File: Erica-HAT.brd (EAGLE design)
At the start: 65 x 56 mm, 64 parts, among them IC1 MEGA8-AI, K1 PIN20X2, Q1 12M, Q2 2.5A/30V, U1 EEPROM24, U2 TMP102, U3 AD5241BRZ1M, U4 MMDT2907A-7-F, U5 +12v

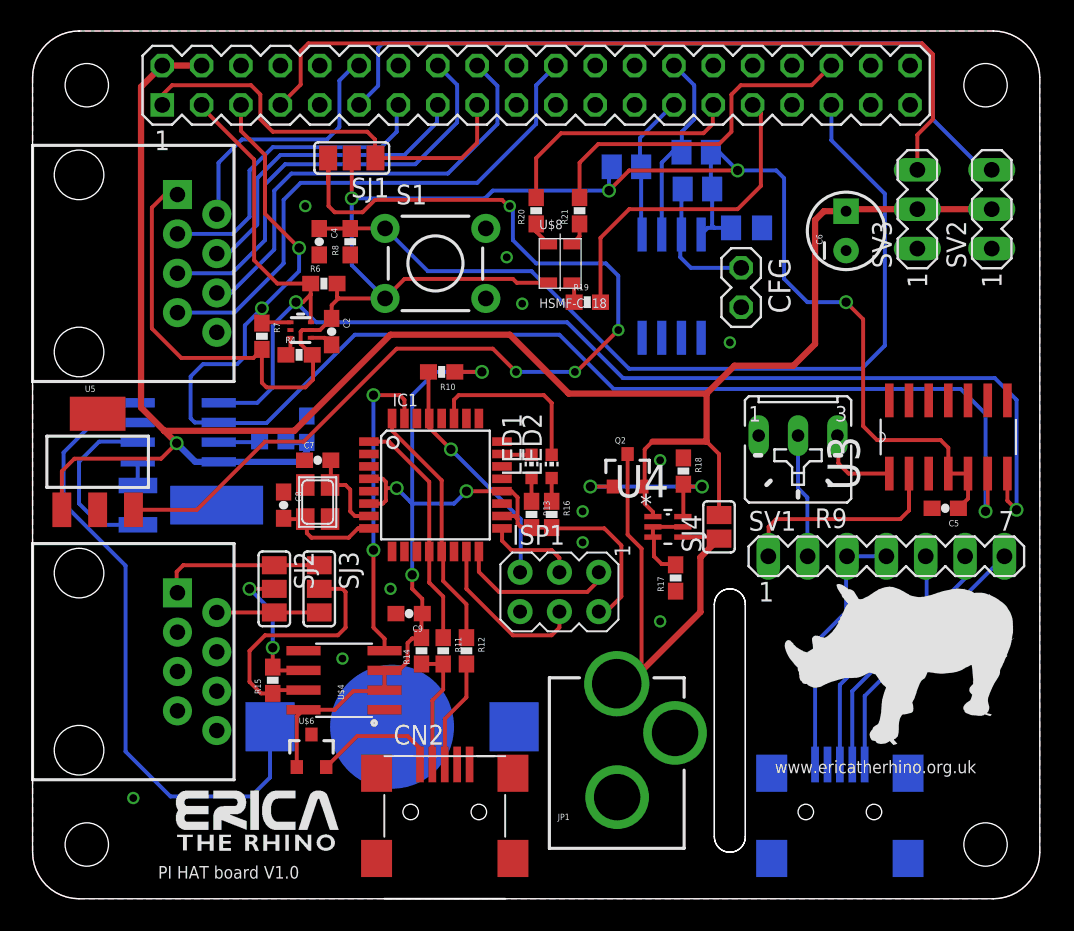
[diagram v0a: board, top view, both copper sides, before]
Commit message: Fixed remaining air wires. Added additional stitching. DRC clean.
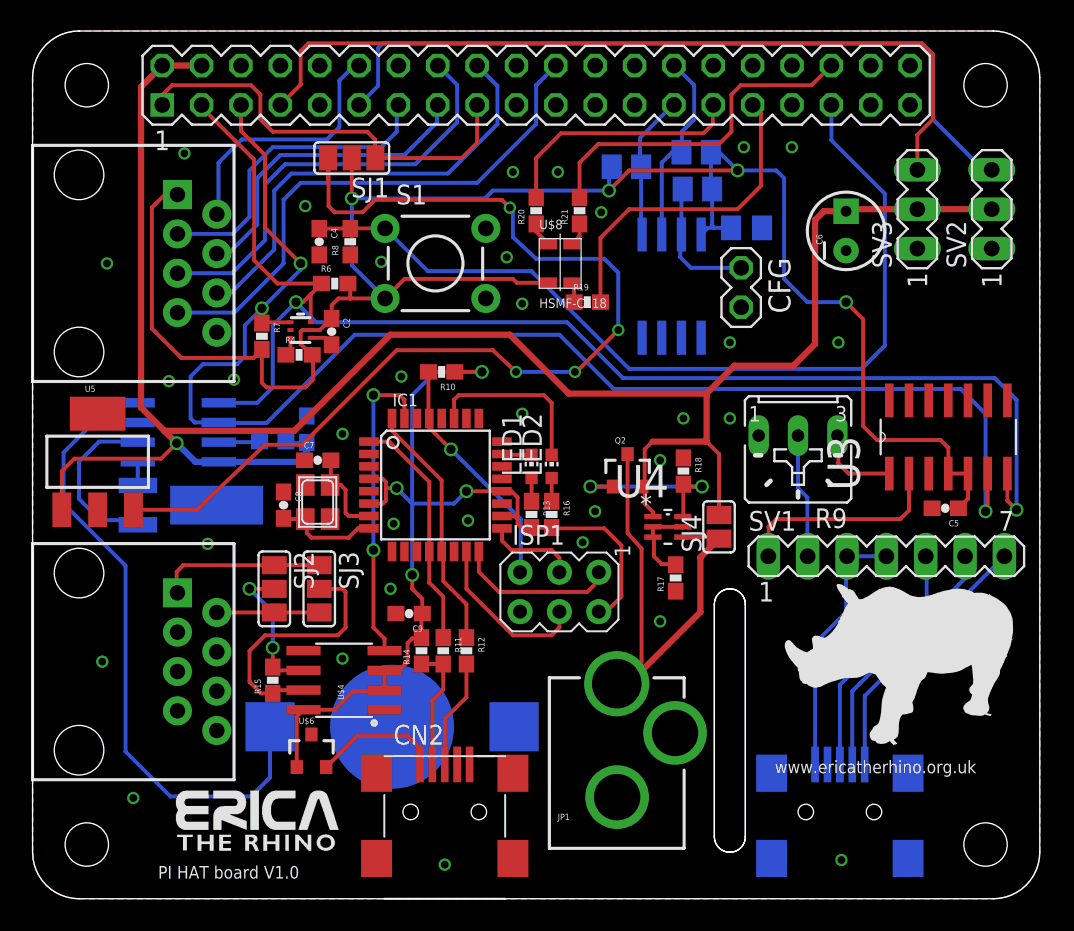
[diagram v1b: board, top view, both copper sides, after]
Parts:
- moved R6 0.70 mm to (19.5, 39.7)
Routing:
- net SDA: track 88.2 -> 89.2 mm
- net GND: vias 12 -> 34
